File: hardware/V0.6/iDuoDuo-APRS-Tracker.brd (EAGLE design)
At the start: 82.8 x 27.1 mm, 41 parts, among them IC1 ATMEGA328, IC2 VHF-MODULE, Q2 SI2301, Q3 SI2301, Q4 SI2302, Q5 SI2302, U1 MCP73831, X1 SMA_ANT, Y1 16MHz

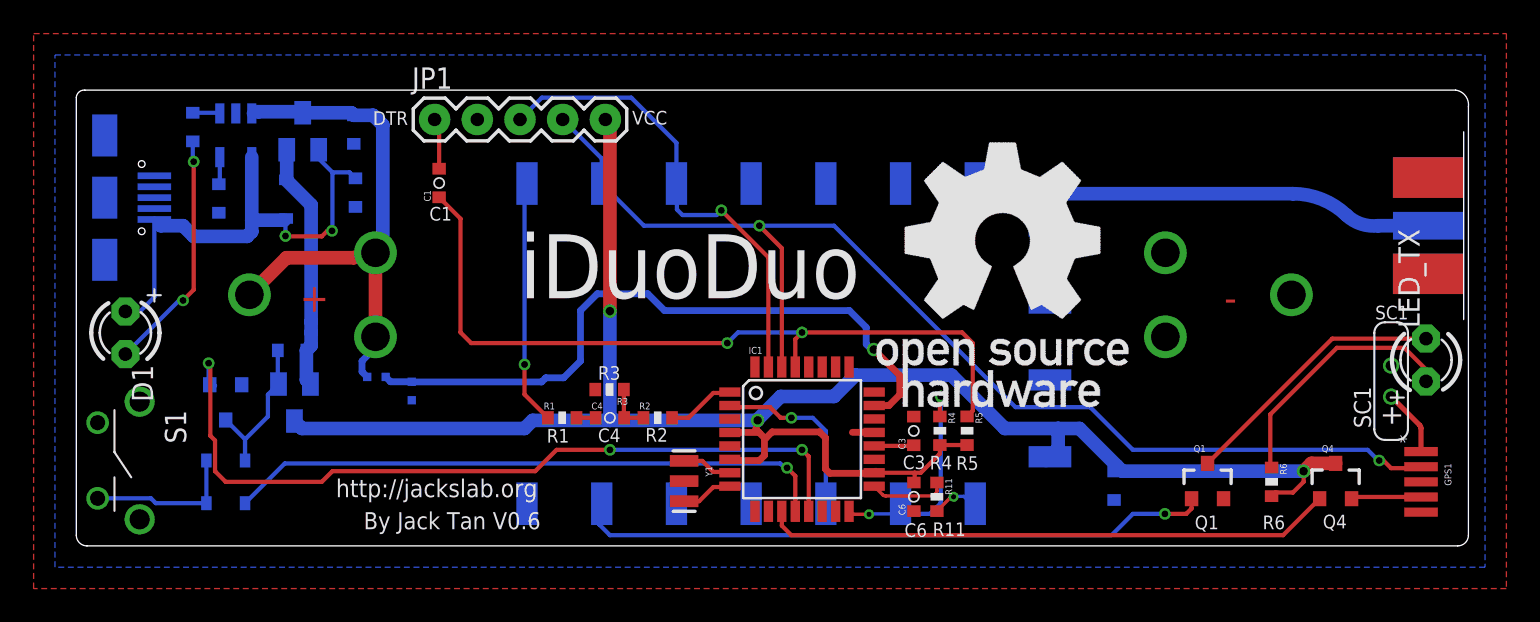
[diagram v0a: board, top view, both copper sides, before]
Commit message: hardware: fix the gps switch bug of v0.6
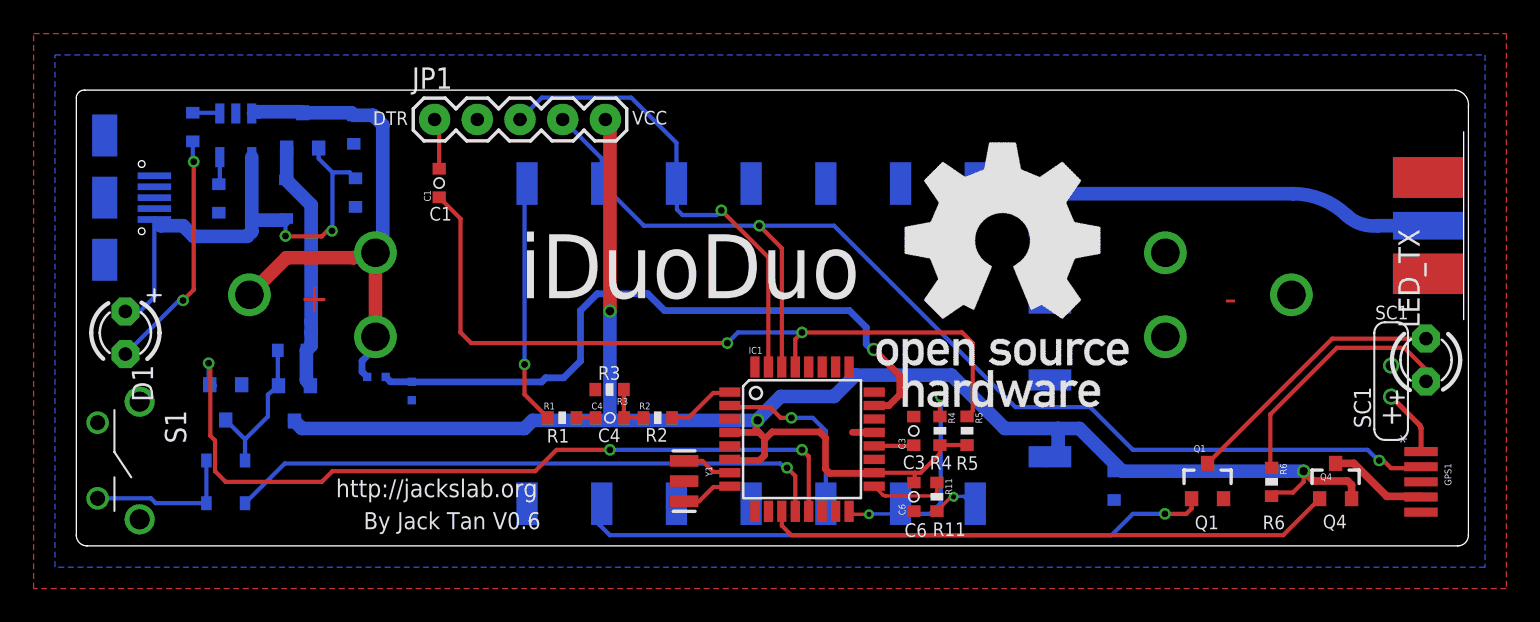
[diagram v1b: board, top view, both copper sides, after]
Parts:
- Q4: value SI2302 -> SI2301; device ehl:SOT23-3 -> ehl:SOT23
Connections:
- removed net PWR_GPS: GPS1.P$4, Q4.2
- new net GPS_PWR: GPS1.P$4, Q4.3
- net VCC: now also Q4.2; no longer Q4.3
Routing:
- net GPS_PWR: track 0.00 -> 5.91 mm
- net PWR_GPS: track 4.17 -> 0.00 mm
- net VCC: track 113.0 -> 114.9 mm
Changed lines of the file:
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@@
 <layer number="59" name="tCarbon" color="7" fill="1" visible="no" active="no"/>
 <layer number="60" name="bCarbon" color="7" fill="1" visible="no" active="no"/>
+<layer number="88" name="SimResults" color="9" fill="1" visible="yes" active="yes"/>
+<layer number="89" name="SimProbes" color="9" fill="1" visible="yes" active="yes"/>
 <layer number="90" name="Modules" color="7" fill="1" visible="no" active="yes"/>
 <layer number="91" name="Nets" color="2" fill="1" visible="no" active="no"/>
@@
 <layer number="113" name="WhiteOver" color="0" fill="1" visible="no" active="yes"/>
 <layer number="114" name="BlackOver" color="15" fill="1" visible="no" active="yes"/>
+<layer number="115" name="FRNTMAAT2" color="7" fill="1" visible="yes" active="yes"/>
 <layer number="116" name="Patch_BOT" color="9" fill="4" visible="no" active="yes"/>
+<layer number="117" name="BACKMAAT1" color="7" fill="1" visible="yes" active="yes"/>
 <layer number="118" name="Rect_Pads" color="7" fill="1" visible="no" active="yes"/>
+<layer number="119" name="KAP_TEKEN" color="7" fill="1" visible="yes" active="yes"/>
+<layer number="120" name="KAP_MAAT1" color="7" fill="1" visible="yes" active="yes"/>
 <layer number="121" name="_tsilk" color="7" fill="1" visible="no" active="yes"/>
 <layer number="122" name="_bsilk" color="7" fill="1" visible="no" active="yes"/>
@@
 <layer number="128" name="_bValues" color="7" fill="1" visible="no" active="yes"/>
 <layer number="129" name="Mask" color="7" fill="1" visible="no" active="yes"/>
+<layer number="130" name="SMDSTROOK" color="7" fill="1" visible="yes" active="yes"/>
 <layer number="131" name="prix" color="7" fill="1" visible="no" active="yes"/>
 <layer number="132" name="test" color="7" fill="1" visible="no" active="yes"/>
+<layer number="133" name="bottom_silk" color="7" fill="1" visible="yes" active="yes"/>
+<layer number="134" name="silk_top" color="7" fill="1" visible="yes" active="yes"/>
+<layer number="135" name="silk_bottom" color="7" fill="1" visible="yes" active="yes"/>
+<layer number="136" name="silktop" color="7" fill="1" visible="yes" active="yes"/>
+<layer number="137" name="silkbottom" color="7" fill="1" visible="yes" active="yes"/>
 <layer number="144" name="Drill_legend" color="7" fill="1" visible="no" active="yes"/>
+<layer number="145" name="DrillLegend_01-16" color="7" fill="1" visible="yes" active="yes"/>
+<layer number="146" name="DrillLegend_01-20" color="7" fill="1" visible="yes" active="yes"/>
 <layer number="150" name="Notes" color="7" fill="1" visible="no" active="yes"/>
 <layer number="151" name="HeatSink" color="7" fill="1" visible="no" active="yes"/>
@@
 <element name="R9" library="ehl" package="0603-RES" value="10K" x="16.61" y="21.02" rot="MR90"/>
 <element name="Q3" library="ehl" package="SOT23" value="SI2301" x="12.98" y="8.53" rot="MR180"/>
-<element name="Q4" library="ehl" package="SOT23-3" value="SI2302" x="74.93" y="3.81"/>
+<element name="Q4" library="ehl" package="SOT23" value="SI2301" x="74.93" y="3.81"/>
 <element name="R10" library="ehl" package="0603-RES" value="1M" x="12.84" y="11.63" rot="MR180"/>
 <element name="D3" library="ehl" package="SOD-323" value="" x="8.89" y="2.54" rot="MR180"/>
@@
 <contactref element="R4" pad="2"/>
 <contactref element="R6" pad="2"/>
-<contactref element="Q4" pad="3"/>
 <contactref element="Q3" pad="3"/>
 <wire x1="51.3844" y1="5.4866" x2="51.3844" y2="5.999" width="0.254" layer="1"/>
@@
 <wire x1="62.23" y1="4.445" x2="73.025" y2="4.445" width="0.8128" layer="16"/>
 <via x="73.025" y="4.445" extent="1-16" drill="0.5"/>
-<wire x1="73.025" y1="4.445" x2="73.49" y2="4.91" width="0.8128" layer="1"/>
-<wire x1="73.49" y1="4.91" x2="74.93" y2="4.91" width="0.8128" layer="1"/>
 <wire x1="71.12" y1="2.96" x2="71.335" y2="3.175" width="0.254" layer="1"/>
 <wire x1="71.335" y1="3.175" x2="72.39" y2="3.175" width="0.254" layer="1"/>
@@
 <wire x1="61.83810625" y1="4.52210625" x2="61.9125" y2="4.701709375" width="0.2032" layer="16" curve="44.999295"/>
 <wire x1="61.9125" y1="4.701709375" x2="61.9125" y2="4.7625" width="0.2032" layer="16"/>
+<contactref element="Q4" pad="2"/>
+<wire x1="75.88" y1="2.81" x2="75.88" y2="3.622" width="0.4572" layer="1"/>
+<wire x1="75.88" y1="3.622" x2="75.6412" y2="3.8608" width="0.4572" layer="1"/>
+<wire x1="75.6412" y1="3.8608" x2="73.6092" y2="3.8608" width="0.4572" layer="1"/>
+<wire x1="73.6092" y1="3.8608" x2="73.025" y2="4.445" width="0.4572" layer="1"/>
 </signal>
 <signal name="A0">
@@
 <wire x1="16.255" y1="22.225" x2="15.24" y2="22.225" width="0.254" layer="16"/>
 <wire x1="15.24" y1="22.225" x2="14.42" y2="23.045" width="0.254" layer="16"/>
-<wire x1="14.42" y1="23.045" x2="14.42" y2="23.57" width="0.254" layer="16"/>
+<wire x1="14.42" y1="23.045" x2="14.42" y2="23.67" width="0.254" layer="16"/>
 <wire x1="10.44" y1="23.1299" x2="10.414" y2="23.1039" width="0.254" layer="16"/>
 <wire x1="4.644" y1="19.42" x2="4.9632" y2="19.1008" width="0.4064" layer="16"/>
@@
 <wire x1="8.54" y1="21.58" x2="8.54" y2="23.1299" width="0.254" layer="16"/>
 </signal>
-<signal name="PWR_GPS">
-<contactref element="GPS1" pad="P$4"/>
-<contactref element="Q4" pad="2"/>
-<wire x1="75.88" y1="2.81" x2="75.98" y2="2.91" width="0.254" layer="1"/>
-<wire x1="75.98" y1="2.91" x2="80.01" y2="2.91" width="0.254" layer="1"/>
-</signal>
 <signal name="VIN">
 <contactref element="Q2" pad="2"/>
@@
 <contactref element="R10" pad="2"/>
 <wire x1="12.48" y1="21.78" x2="12.52" y2="21.82" width="0.254" layer="16"/>
-<wire x1="12.52" y1="21.82" x2="12.52" y2="23.57" width="0.8128" layer="16"/>
+<wire x1="12.52" y1="21.82" x2="12.52" y2="23.67" width="0.8128" layer="16"/>
 <wire x1="12.48" y1="21.78" x2="13.97" y2="20.29" width="0.8128" layer="16"/>
 <wire x1="13.97" y1="20.29" x2="13.97" y2="13.335" width="0.8128" layer="16"/>
 <wire x1="13.97" y1="13.335" x2="13.97" y2="12.7" width="0.8128" layer="16"/>
-<wire x1="13.93" y1="9.63" x2="13.69" y2="9.87" width="0.8128" layer="16"/>
+<wire x1="13.93" y1="9.53" x2="13.69" y2="9.87" width="0.8128" layer="16"/>
 <wire x1="13.69" y1="9.87" x2="13.69" y2="11.63" width="0.8128" layer="16"/>
 <wire x1="13.69" y1="11.63" x2="13.97" y2="11.91" width="0.8128" layer="16"/>
@@
 <wire x1="8.89" y1="7.49" x2="10.04" y2="6.34" width="0.254" layer="16"/>
 <wire x1="10.04" y1="6.34" x2="10.04" y2="5.08" width="0.254" layer="16"/>
-<wire x1="12.03" y1="9.63" x2="11.99" y2="9.67" width="0.254" layer="16"/>
+<wire x1="12.03" y1="9.53" x2="11.99" y2="9.67" width="0.254" layer="16"/>
 <wire x1="11.99" y1="9.67" x2="11.99" y2="11.63" width="0.254" layer="16"/>
-<wire x1="12.03" y1="9.63" x2="11.4" y2="9" width="0.254" layer="16"/>
+<wire x1="12.03" y1="9.53" x2="11.4" y2="9" width="0.254" layer="16"/>
 <wire x1="11.4" y1="9" x2="11.4" y2="7.7" width="0.254" layer="16"/>
 <wire x1="11.4" y1="7.7" x2="10.04" y2="6.34" width="0.254" layer="16"/>
@@
 <wire x1="80.01" y1="6.996190625" x2="80.01" y2="5.61" width="0.3048" layer="1"/>
 </signal>
+<signal name="GPS_PWR">
+<contactref element="GPS1" pad="P$4"/>
+<contactref element="Q4" pad="3"/>
+<wire x1="74.93" y1="4.91" x2="76.0144" y2="4.91" width="0.4572" layer="1"/>
+<wire x1="76.0144" y1="4.91" x2="77.978" y2="2.9464" width="0.4572" layer="1"/>
+<wire x1="77.978" y1="2.9464" x2="79.9736" y2="2.9464" width="0.4572" layer="1"/>
+<wire x1="79.9736" y1="2.9464" x2="80.01" y2="2.91" width="0.4572" layer="1"/>
+</signal>
 </signals>
